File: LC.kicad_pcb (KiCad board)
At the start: 2 copper layers, 60 x 65 mm, 86 parts, among them J1 INPUT+, J10 DISPLAY, J11 ENTER_BUTTON, J12 UP_BUTTON, J2 INPUT-, J3 Barrel_Jack, J4 EXT_CLK, J5 CLKSRC, J6 SIGSRC, J7 EXT_SIG, J8 UNUSED, J9 PROG, Q1 BC817, Q2 BC817, SW1 RESET_BTN, U1 Omron_G2V, U10 74HC590PW,118, U11 74HCS251, U12 AVR32DB28x-xSO, U2 L7805, U3 74AHC1G04, U4 Omron_G2E, U5 74AHC1G14, U6 74AHC1G04, U7 LM311, U8 74AUC1G74, U9 74AUC2G125, Y1 10MHz

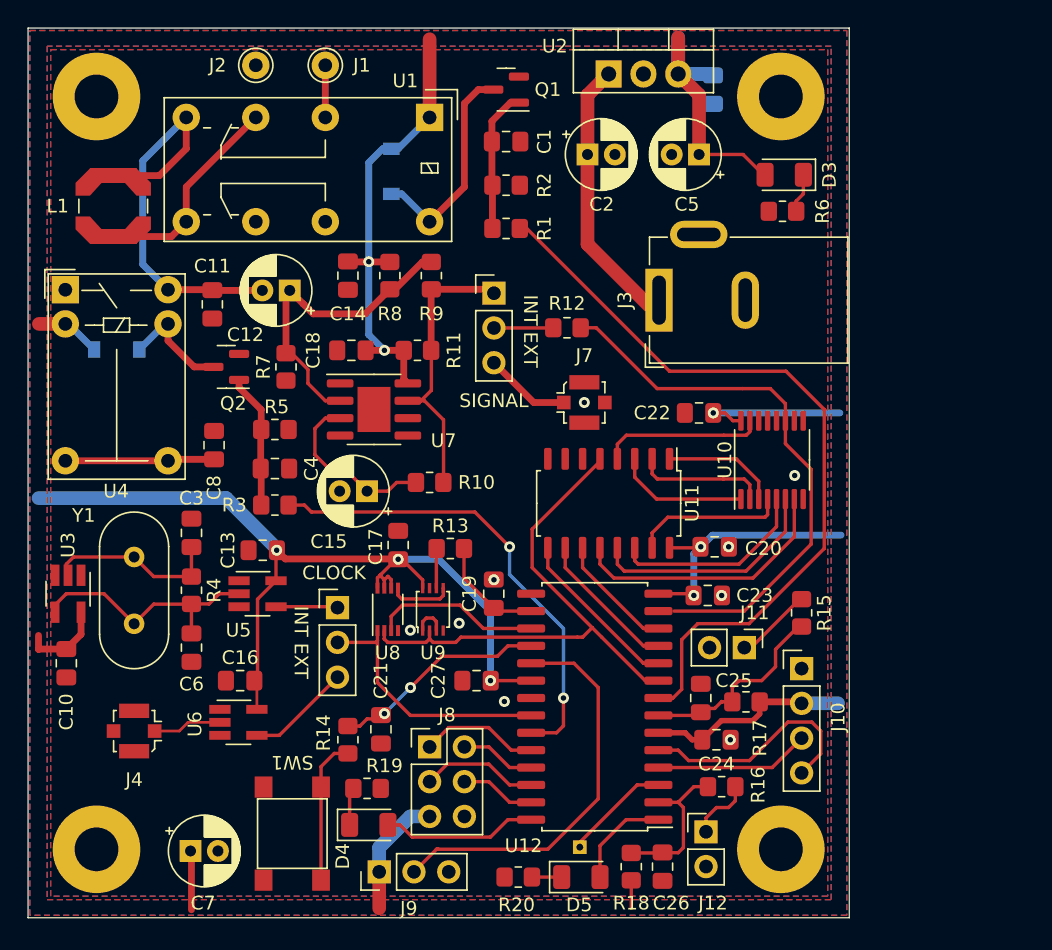
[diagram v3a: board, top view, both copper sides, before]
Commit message: changed comparator: LM311 became TLV3201
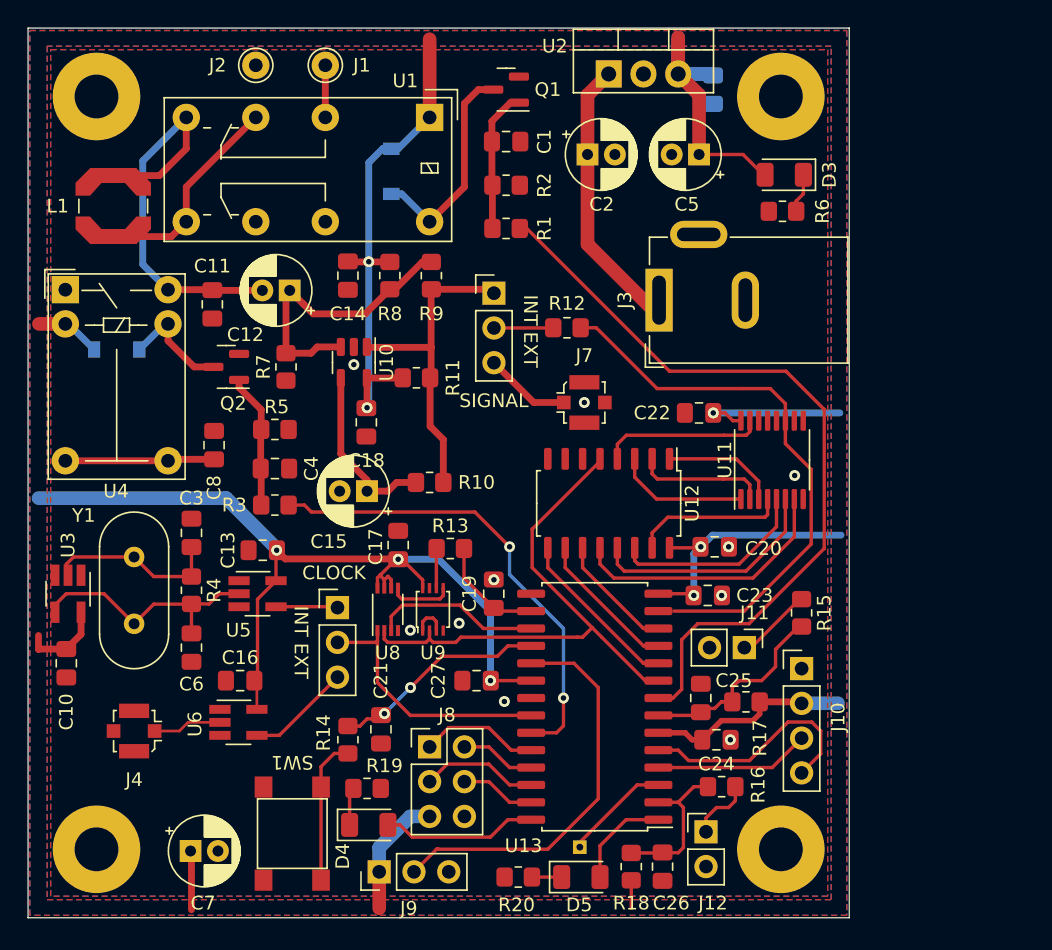
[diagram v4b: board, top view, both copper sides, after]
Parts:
- removed U7: LM311, Package_SO:SOIC-8-1EP_3.9x4.9mm_P1.27mm_EP2.41x3.3mm
- added U10: TLV3201, Package_TO_SOT_SMD:SOT-23-5, F.Cu at (158.8, 59.4)
- moved C18 5.37 mm to (159.7, 63.8), turned to 90 degrees
- moved R11 2.01 mm to (163.4, 60.6)
- renumbered U10 to U11, U11 to U12, U12 to U13
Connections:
- net Net-(C12-Pad1) renamed /IN+
- net Net-(C15-Pad1) renamed /IN-
- net Net-(J6-Pad1) renamed /COMP_OUT
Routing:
- net +5V: track 191.0 -> 194.3 mm
- net /IN+: track 23.3 -> 21.5 mm
- net /COMP_OUT: track 21.9 -> 23.4 mm
- net GND: vias 9 -> 10

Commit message: Update LC.kicad_pcb
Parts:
- moved C15 2.51 mm to (159.0, 66.4), turned to -90 degrees
- moved R10 1.75 mm to (164.3, 66.4)
- moved C18 1.37 mm to (160.8, 62.9), turned to 180 degrees
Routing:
- net /IN-: track 12.9 -> 10.6 mm
- net /COMP_OUT: track 23.4 -> 21.7 mm
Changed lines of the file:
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@@
     (property "Sheetname" "")
     (attr smd)
-    (fp_text reference "R11" (at -2.667 0 90) (layer "F.SilkS")
+    (fp_text reference "R11" (at 0.0508 1.778 180) (layer "F.SilkS")
       (effects (font (size 1 1) (thickness 0.15)))
     )
@@
   )
   (footprint "Capacitor_SMD:C_0805_2012Metric_Pad1.18x1.45mm_HandSolder" (layer "F.Cu")
-    (at 159.7152 63.8048 90)
+    (at 160.782 62.9412 180)
     (descr "Capacitor SMD 0805 (2012 Metric), square (rectangular) end terminal, IPC_7351 nominal with elongated pad for handsoldering. (Body size source: IPC-SM-782 page 76, https://www.pcb-3d.com/wordpress/wp-content/uploads/ipc-sm-782a_amendment_1_and_2.pdf, https://docs.google.com/spreadsheets/d/1BsfQQcO9C6DZCsRaXUlFlo91Tg2WpOkGARC1WS5S8t0/edit?usp=sharing), generated with kicad-footprint-generator")
     (tags "capacitor handsolder")
@@
     (property "Sheetname" "")
     (attr smd)
-    (fp_text reference "C18" (at -2.794 0) (layer "F.SilkS")
+    (fp_text reference "C18" (at -3.4544 0 180) (layer "F.SilkS")
       (effects (font (size 1 1) (thickness 0.15)))
     )
-    (fp_text value "100n" (at 0 1.68 90) (layer "F.Fab")
+    (fp_text value "100n" (at 0 1.68) (layer "F.Fab")
       (effects (font (size 1 1) (thickness 0.15)))
     )
-    (fp_text user "${REFERENCE}" (at 0 0 90) (layer "F.Fab")
+    (fp_text user "${REFERENCE}" (at 0 0) (layer "F.Fab")
       (effects (font (size 0.5 0.5) (thickness 0.08)))
     )
@@
     (fp_line (start 1 0.625) (end -1 0.625) (layer "F.Fab") (width 0.1))
     (fp_line (start -1 -0.625) (end 1 -0.625) (layer "F.Fab") (width 0.1))
-    (pad "1" smd roundrect (at -1.0375 0 90) (size 1.175 1.45) (layers "F.Cu" "F.Paste" "F.Mask") (roundrect_rratio 0.212766)
+    (pad "1" smd roundrect (at -1.0375 0 180) (size 1.175 1.45) (layers "F.Cu" "F.Paste" "F.Mask") (roundrect_rratio 0.212766)
       (net 3 "GND") (pintype "passive"))
-    (pad "2" smd roundrect (at 1.0375 0 90) (size 1.175 1.45) (layers "F.Cu" "F.Paste" "F.Mask") (roundrect_rratio 0.212766)
+    (pad "2" smd roundrect (at 1.0375 0 180) (size 1.175 1.45) (layers "F.Cu" "F.Paste" "F.Mask") (roundrect_rratio 0.212766)
       (net 26 "+5V") (pintype "passive"))
     (model "${KICAD6_3DMODEL_DIR}/Capacitor_SMD.3dshapes/C_0805_2012Metric.wrl"
@@
   )
   (footprint "Resistor_SMD:R_0805_2012Metric_Pad1.20x1.40mm_HandSolder" (layer "F.Cu")
-    (at 164.338 68.199)
+    (at 164.2872 66.4464)
     (descr "Resistor SMD 0805 (2012 Metric), square (rectangular) end terminal, IPC_7351 nominal with elongated pad for handsoldering. (Body size source: IPC-SM-782 page 72, https://www.pcb-3d.com/wordpress/wp-content/uploads/ipc-sm-782a_amendment_1_and_2.pdf), generated with kicad-footprint-generator")
     (tags "resistor handsolder")
@@
     (property "Sheetname" "")
     (attr smd)
-    (fp_text reference "U10" (at 0 -2.4 90) (layer "F.SilkS")
+    (fp_text reference "U10" (at 0.1016 2.4892 90) (layer "F.SilkS")
       (effects (font (size 1 1) (thickness 0.15)))
     )
@@
   )
   (footprint "Capacitor_THT:CP_Radial_D5.0mm_P2.00mm" (layer "F.Cu")
-    (at 159.766 68.834 180)
+    (at 159.004 66.4464 -90)
     (descr "CP, Radial series, Radial, pin pitch=2.00mm, , diameter=5mm, Electrolytic Capacitor")
     (tags "CP Radial series Radial pin pitch 2.00mm  diameter 5mm Electrolytic Capacitor")
@@
     (property "Sheetname" "")
     (attr through_hole)
-    (fp_text reference "C15" (at 2.794 -3.683 180) (layer "F.SilkS")
+    (fp_text reference "C15" (at 2.794 -3.683 90) (layer "F.SilkS")
       (effects (font (size 1 1) (thickness 0.15)))
     )
-    (fp_text value "10u" (at 1 3.75) (layer "F.Fab")
+    (fp_text value "10u" (at 1 3.75 -270) (layer "F.Fab")
       (effects (font (size 1 1) (thickness 0.15)))
     )
-    (fp_text user "${REFERENCE}" (at 1 0) (layer "F.Fab")
+    (fp_text user "${REFERENCE}" (at 1 0 -270) (layer "F.Fab")
       (effects (font (size 1 1) (thickness 0.15)))
     )
@@
     (fp_line (start -0.883605 -1.3375) (end -0.883605 -0.8375) (layer "F.Fab") (width 0.1))
     (fp_circle (center 1 0) (end 3.5 0) (layer "F.Fab") (width 0.1) (fill none))
-    (pad "1" thru_hole rect (at 0 0 180) (size 1.6 1.6) (drill 0.8) (layers *.Cu *.Mask)
+    (pad "1" thru_hole rect (at 0 0 270) (size 1.6 1.6) (drill 0.8) (layers *.Cu *.Mask)
       (net 68 "/IN-") (pintype "passive"))
-    (pad "2" thru_hole circle (at 2 0 180) (size 1.6 1.6) (drill 0.8) (layers *.Cu *.Mask)
+    (pad "2" thru_hole circle (at 2 0 270) (size 1.6 1.6) (drill 0.8) (layers *.Cu *.Mask)
       (net 3 "GND") (pintype "passive"))
     (model "${KICAD6_3DMODEL_DIR}/Capacitor_THT.3dshapes/CP_Radial_D5.0mm_P2.00mm.wrl"
@@
   (segment (start 136.845 77.277) (end 137.795 76.327) (width 0.25) (layer "F.Cu") (net 10))
   (segment (start 142.748 78.523) (end 144.182 77.089) (width 0.25) (layer "F.Cu") (net 10))
-  (segment (start 154.035 69.85) (end 155.194 69.85) (width 0.25) (layer "F.Cu") (net 11))
   (segment (start 173.609 86.487) (end 171.753 86.487) (width 0.25) (layer "F.Cu") (net 11))
-  (segment (start 155.194 69.85) (end 155.702 70.358) (width 0.25) (layer "F.Cu") (net 11))
   (segment (start 174.117 85.979) (end 173.609 86.487) (width 0.25) (layer "F.Cu") (net 11))
   (segment (start 174.117 83.947) (end 174.117 85.979) (width 0.25) (layer "F.Cu") (net 11))
-  (segment (start 155.702 70.358) (end 167.64 70.358) (width 0.25) (layer "F.Cu") (net 11))
-  (segment (start 167.64 70.358) (end 170.18 72.898) (width 0.25) (layer "F.Cu") (net 11))
+  (segment (start 154.035 69.85) (end 167.132 69.85) (width 0.25) (layer "F.Cu") (net 11))
+  (segment (start 167.132 69.85) (end 170.18 72.898) (width 0.25) (layer "F.Cu") (net 11))
   (via (at 170.18 72.898) (size 0.8) (drill 0.4) (layers "F.Cu" "B.Cu") (net 11))
   (via (at 174.117 83.947) (size 0.8) (drill 0.4) (layers "F.Cu" "B.Cu") (net 11))
@@
   (segment (start 163.814 52.086) (end 161.814 54.086) (width 0.5) (layer "F.Cu") (net 67))
   (segment (start 153.844 58.756) (end 155.6708 58.756) (width 0.5) (layer "F.Cu") (net 67))
-  (segment (start 159.766 68.834) (end 161.29 68.834) (width 0.5) (layer "F.Cu") (net 68))
-  (segment (start 159.766 68.834) (end 159.766 68.0212) (width 0.5) (layer "F.Cu") (net 68))
-  (segment (start 159.766 68.0212) (end 157.8508 66.106) (width 0.5) (layer "F.Cu") (net 68))
-  (segment (start 157.8508 66.106) (end 157.8508 60.5735) (width 0.5) (layer "F.Cu") (net 68))
-  (segment (start 161.29 68.834) (end 161.925 68.199) (width 0.5) (layer "F.Cu") (net 68))
-  (segment (start 161.925 68.199) (end 163.338 68.199) (width 0.5) (layer "F.Cu") (net 68))
+  (segment (start 157.8508 65.2932) (end 159.004 66.4464) (width 0.5) (layer "F.Cu") (net 68))
+  (segment (start 159.004 66.4464) (end 163.2872 66.4464) (width 0.5) (layer "F.Cu") (net 68))
+  (segment (start 157.8508 60.5735) (end 157.8508 65.2932) (width 0.5) (layer "F.Cu") (net 68))
   (segment (start 164.3728 64.0936) (end 165.338 65.0588) (width 0.5) (layer "F.Cu") (net 69))
   (segment (start 159.7801 58.3278) (end 159.7508 58.2985) (width 0.5) (layer "F.Cu") (net 69))
   (segment (start 164.3728 60.5536) (end 164.3728 64.0936) (width 0.5) (layer "F.Cu") (net 69))
   (segment (start 164.449 54.102) (end 164.449 58.3278) (width 0.5) (layer "F.Cu") (net 69))
+  (segment (start 165.338 66.3956) (end 165.2872 66.4464) (width 0.5) (layer "F.Cu") (net 69))
   (segment (start 168.752 54.086) (end 169.037 54.371) (width 0.5) (layer "F.Cu") (net 69))
   (segment (start 164.449 58.3278) (end 159.7801 58.3278) (width 0.5) (layer "F.Cu") (net 69))
@@
   (segment (start 164.465 54.086) (end 164.449 54.102) (width 0.5) (layer "F.Cu") (net 69))
   (segment (start 164.449 58.3278) (end 164.449 60.0202) (width 0.5) (layer "F.Cu") (net 69))
-  (segment (start 165.338 65.0588) (end 165.338 68.199) (width 0.5) (layer "F.Cu") (net 69))
+  (segment (start 165.338 65.0588) (end 165.338 66.3956) (width 0.5) (layer "F.Cu") (net 69))
   (zone (net 3) (net_name "GND") (layers F&B.Cu) (hatch edge 0.508)
     (connect_pads (clearance 0))

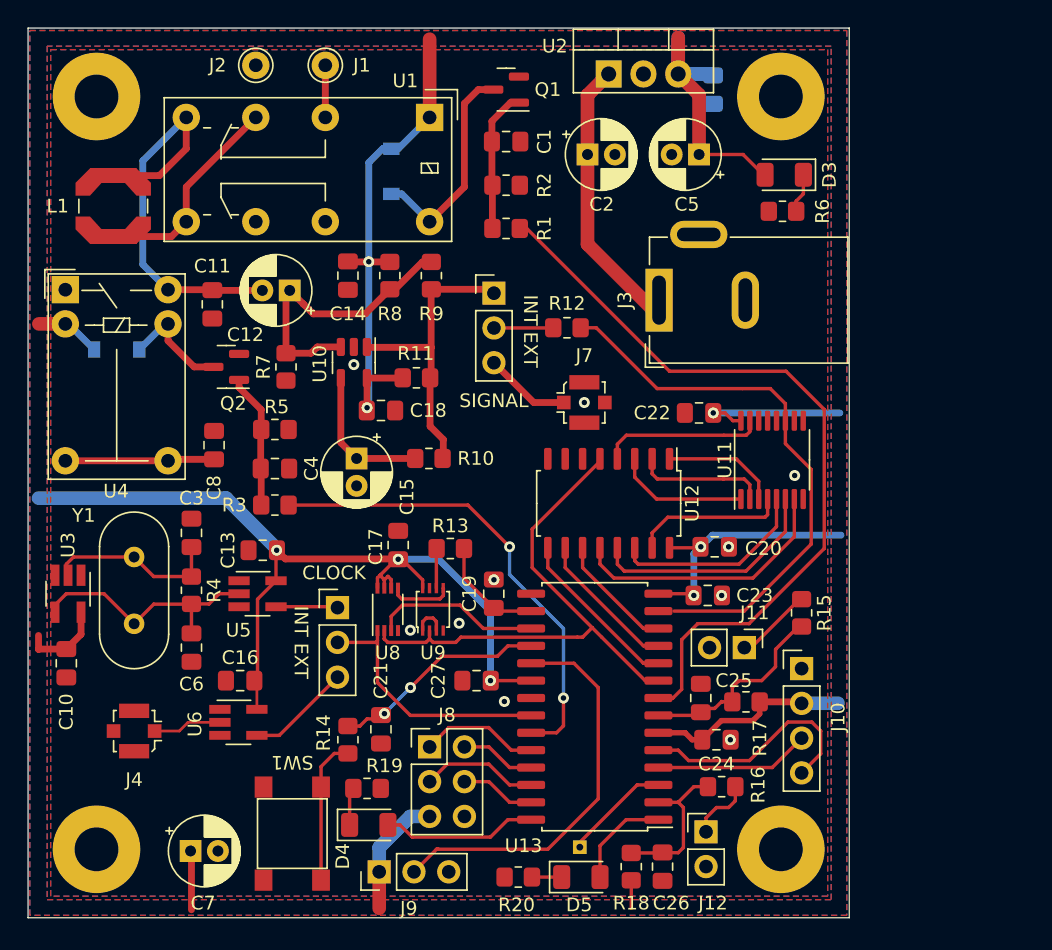
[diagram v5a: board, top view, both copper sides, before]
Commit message: Updated comparator oscillator with LTSpice simulation results
LT1719 operates nicely, but some values need to be adjusted. Especially the coupling caps need to be changed (10u -> 1u) so I decided to change them to MLCC.
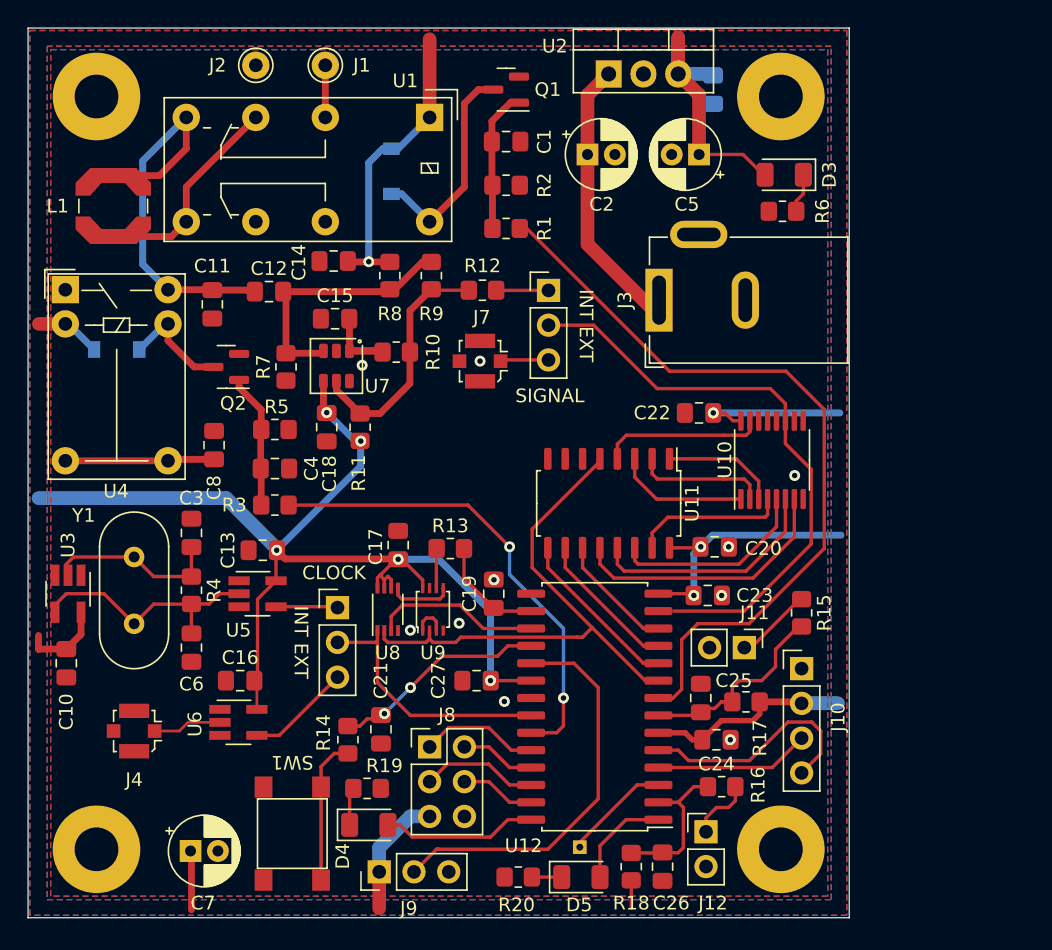
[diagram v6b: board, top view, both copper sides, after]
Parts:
- removed the U10 at (158.8, 59.4)
- added U7: LT1719CS6, Package_TO_SOT_SMD_AKL:SOT-23-6, F.Cu at (157.5, 59.7)
- C12, C15: value 10u -> 1u; footprint Capacitor_THT:CP_Radial_D5.0mm_P2.00mm -> Capacitor_SMD:C_0805_2012Metric_Pad1.18x1.45mm_HandSolder
- R10: value 47k -> 68k
- R11: value 1k -> 1k DNP
- R8, R9: value 100k -> 120k
- moved C15 10.3 mm to (157.4, 56.2), turned to 0 degrees
- moved J7 8.20 mm to (168.0, 59.3), turned to 90 degrees
- moved R10 8.13 mm to (161.9, 58.7)
- moved R12 6.75 mm to (168.2, 54.2), turned to 180 degrees
- moved R11 5.47 mm to (159.3, 64.2), turned to -90 degrees
- moved C18 4.15 mm to (156.8, 64.2), turned to 90 degrees
- moved J6 3.99 mm to (173.0, 54.2)
- moved C12 1.52 mm to (152.6, 54.3), turned to 0 degrees
- moved C14 1.49 mm to (157.3, 52.0), turned to 0 degrees
- renumbered U11 to U10, U12 to U11, U13 to U12
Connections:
- C12 pad 1: /IN+ -> Net-(C11-Pad2)
- C12 pad 2: Net-(C11-Pad2) -> Net-(R7-Pad2)
- C15 pad 1: /IN- -> GND
- C15 pad 2: GND -> Net-(R10-Pad1)
- J6 pad 1: /COMP_OUT -> Net-(J6-Pad1)
- J6 pad 2: Net-(J6-Pad2) -> /SIG_OUT
- R10 pad 1: /IN- -> Net-(R10-Pad1)
- R10 pad 2: /COMP_OUT -> Net-(R10-Pad2)
- R11 pad 1: /COMP_OUT -> Net-(R10-Pad2)
- R12 pad 1: Net-(J6-Pad2) -> Net-(J6-Pad1)
- R12 pad 2: /SIG_OUT -> Net-(R10-Pad2)
- R7 pad 2: /IN+ -> Net-(R7-Pad2)
- R8 pad 1: /IN+ -> Net-(R7-Pad2)
- R9 pad 1: /IN+ -> Net-(R7-Pad2)
- R9 pad 2: /COMP_OUT -> Net-(R10-Pad2)
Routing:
- net /COMP_OUT: track 21.7 -> 0.00 mm
- net /IN+: track 21.5 -> 0.00 mm
- net Net-(R7-Pad2): track 0.00 -> 18.7 mm
- net Net-(R10-Pad2): track 0.00 -> 17.9 mm
- net /IN-: track 10.6 -> 0.00 mm
- net Net-(R10-Pad1): track 0.00 -> 7.47 mm
- net Net-(J6-Pad2): track 4.34 -> 0.00 mm
- net Net-(J6-Pad1): track 0.00 -> 3.83 mm
- net Net-(J6-Pad3): track 6.31 -> 3.54 mm
- net /SIG_OUT: track 40.3 -> 42.8 mm
- net Net-(C11-Pad2): track 30.0 -> 29.0 mm
- net +5V: track 194.3 -> 194.8 mm, vias 8 -> 9
